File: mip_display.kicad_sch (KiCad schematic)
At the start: 16 parts, among them IC21 LSF0204GU12X, J5 1-2328702-0, J6 2328702-4, Q4 BC847

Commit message: Changed hand soldered footprints to normal footprints
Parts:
- C79, C82, C85, C86: footprint Capacitor_SMD:C_0603_1608Metric_Pad1.08x0.95mm_HandSolder -> Capacitor_SMD:C_0603_1608Metric
- C80, C81, C84: footprint Capacitor_SMD:C_0402_1005Metric_Pad0.74x0.62mm_HandSolder -> Capacitor_SMD:C_0402_1005Metric
- R46: footprint Resistor_SMD:R_0402_1005Metric_Pad0.72x0.64mm_HandSolder -> Resistor_SMD:R_0402_1005Metric
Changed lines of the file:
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@@
 			)
 		)
-		(property "Footprint" "Capacitor_SMD:C_0402_1005Metric_Pad0.74x0.62mm_HandSolder"
+		(property "Footprint" "Capacitor_SMD:C_0402_1005Metric"
 			(at 200.9648 125.73 0)
 			(effects
@@
 			)
 		)
-		(property "Footprint" "Capacitor_SMD:C_0402_1005Metric_Pad0.74x0.62mm_HandSolder"
+		(property "Footprint" "Capacitor_SMD:C_0402_1005Metric"
 			(at 150.1648 115.57 0)
 			(effects
@@
 			)
 		)
-		(property "Footprint" "Capacitor_SMD:C_0603_1608Metric_Pad1.08x0.95mm_HandSolder"
+		(property "Footprint" "Capacitor_SMD:C_0603_1608Metric"
 			(at 137.4648 115.57 0)
 			(effects
@@
 			)
 		)
-		(property "Footprint" "Capacitor_SMD:C_0402_1005Metric_Pad0.74x0.62mm_HandSolder"
+		(property "Footprint" "Capacitor_SMD:C_0402_1005Metric"
 			(at 80.9752 132.08 0)
 			(effects
@@
 			)
 		)
-		(property "Footprint" "Capacitor_SMD:C_0603_1608Metric_Pad1.08x0.95mm_HandSolder"
+		(property "Footprint" "Capacitor_SMD:C_0603_1608Metric"
 			(at 90.4748 124.46 0)
 			(effects
@@
 			)
 		)
-		(property "Footprint" "Capacitor_SMD:C_0603_1608Metric_Pad1.08x0.95mm_HandSolder"
+		(property "Footprint" "Capacitor_SMD:C_0603_1608Metric"
 			(at 101.9048 124.46 0)
 			(effects
@@
 			)
 		)
-		(property "Footprint" "Capacitor_SMD:C_0603_1608Metric_Pad1.08x0.95mm_HandSolder"
+		(property "Footprint" "Capacitor_SMD:C_0603_1608Metric"
 			(at 212.3948 125.73 0)
 			(effects
@@
 			)
 		)
-		(property "Footprint" "Resistor_SMD:R_0402_1005Metric_Pad0.72x0.64mm_HandSolder"
+		(property "Footprint" "Resistor_SMD:R_0402_1005Metric"
 			(at 100.33 71.882 90)
 			(effects

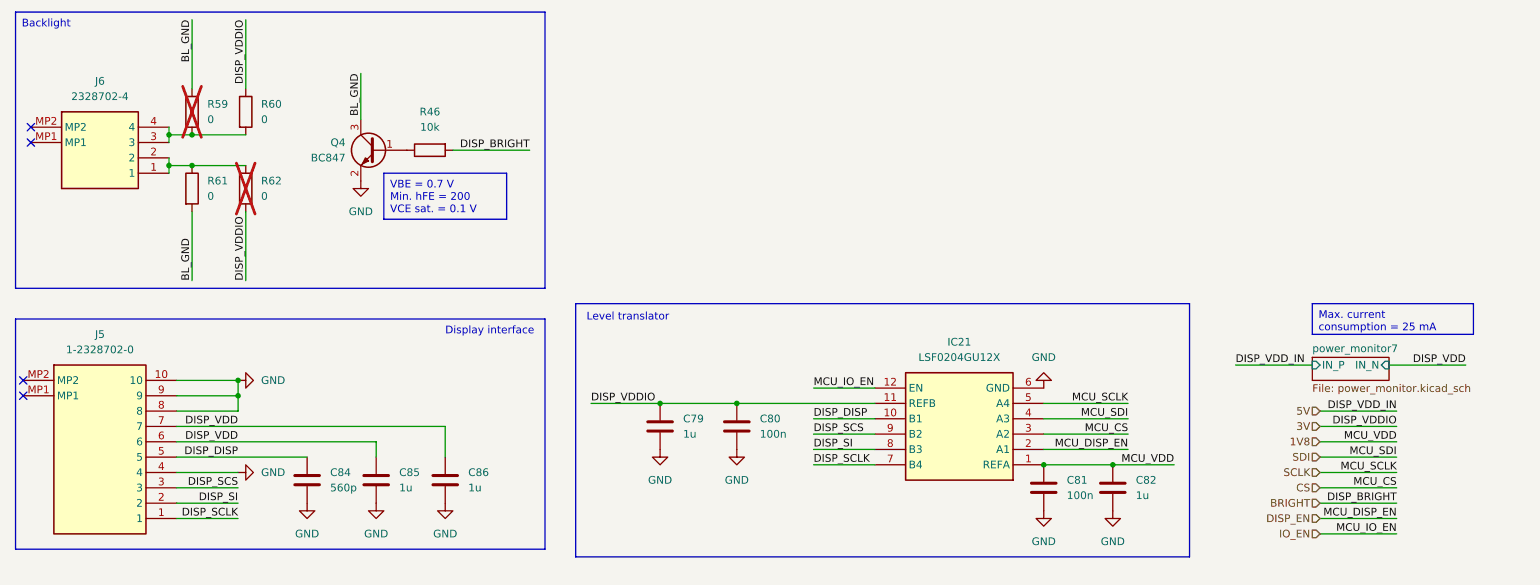
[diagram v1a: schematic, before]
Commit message: Remove RF netclass from a net in gps sheet; Monitor DISP_VDDIO instead of DISP_VDD; Correct constraints
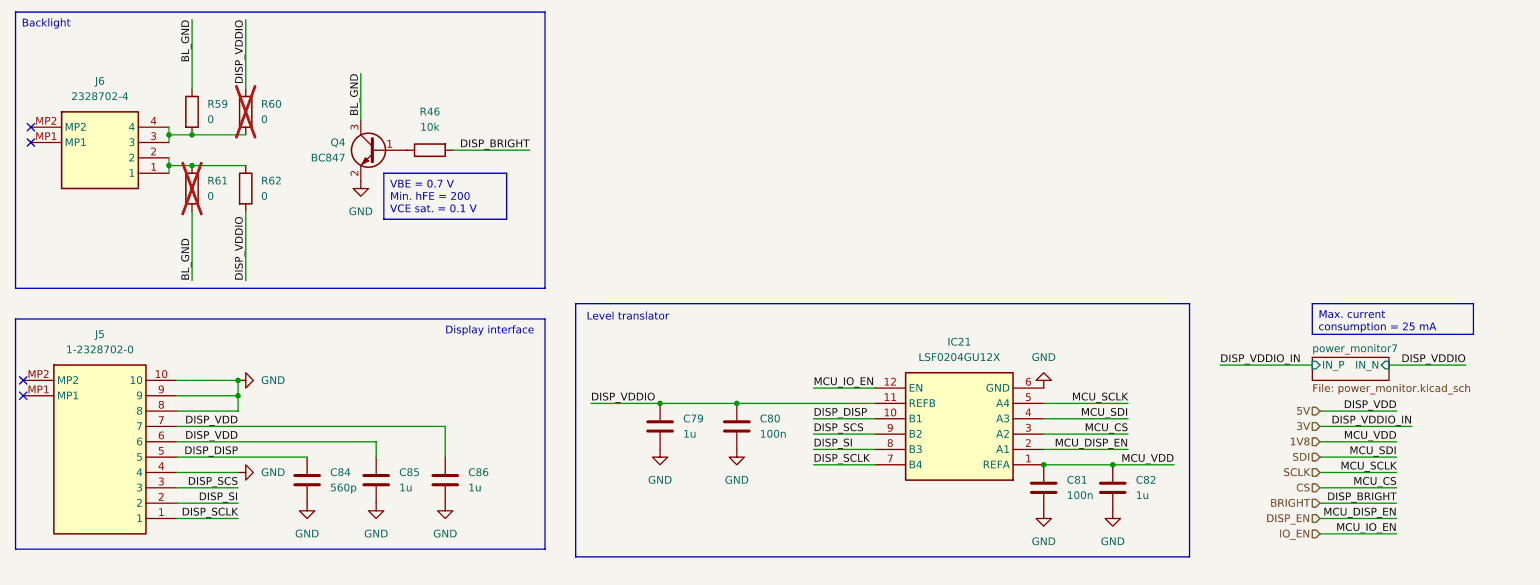
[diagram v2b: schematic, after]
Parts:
- R59, R62: now fitted
- R60, R61: now not fitted
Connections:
- net DISP_VDD is gone; now on net 5V: C85.2, C86.2, J5.6, J5.7
- net 3V: no longer C79.2, C80.2, IC21.11 (REFB), R60.1, R62.2
- new net DISP_VDDIO: C79.2, C80.2, IC21.11 (REFB), R60.1, R62.2
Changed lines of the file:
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@@
 	(wire
 		(pts
-			(xy 233.68 109.22) (xy 246.38 109.22)
+			(xy 231.14 109.22) (xy 246.38 109.22)
 		)
 		(stroke
@@
 	(wire
 		(pts
-			(xy 247.65 119.38) (xy 260.35 119.38)
+			(xy 247.65 119.38) (xy 262.89 119.38)
 		)
 		(stroke
@@
 		)
 	)
-	(label "DISP_VDD"
+	(label "DISP_VDDIO"
 		(at 271.78 109.22 180)
 		(fields_autoplaced yes)
@@
 		)
 	)
-	(label "DISP_VDD_IN"
-		(at 233.68 109.22 0)
+	(label "DISP_VDDIO_IN"
+		(at 231.14 109.22 0)
 		(fields_autoplaced yes)
 		(effects
@@
 		)
 	)
-	(label "DISP_VDD_IN"
+	(label "DISP_VDD"
 		(at 260.35 116.84 180)
 		(fields_autoplaced yes)
@@
 		)
 	)
-	(label "DISP_VDDIO"
-		(at 260.35 119.38 180)
+	(label "DISP_VDDIO_IN"
+		(at 262.89 119.38 180)
 		(fields_autoplaced yes)
 		(effects
@@
 		(in_bom yes)
 		(on_board yes)
-		(dnp no)
+		(dnp yes)
 		(fields_autoplaced yes)
 		(property "Reference" "R61"
@@
 		(in_bom yes)
 		(on_board yes)
-		(dnp yes)
+		(dnp no)
 		(fields_autoplaced yes)
 		(property "Reference" "R62"
@@
 		(in_bom yes)
 		(on_board yes)
-		(dnp no)
+		(dnp yes)
 		(fields_autoplaced yes)
 		(property "Reference" "R60"
@@
 		(in_bom yes)
 		(on_board yes)
-		(dnp yes)
+		(dnp no)
 		(fields_autoplaced yes)
 		(property "Reference" "R59"

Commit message: Finished hardware design
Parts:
- removed J5: 1-2328702-0, 1-2328702-0:123287020, symbol 1-2328702-0:1-2328702-0
- removed J6: 2328702-4, 2328702-4:23287024, symbol 2328702-4:2328702-4
- added J3: 1-2328702-0, 1-2328702-0:123287020, symbol 1-2328702-0:1-2328702-0
- added J4: 2328702-4, 2328702-4:23287024, symbol 2328702-4:2328702-4
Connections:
- net 5V: now also J3.4, J3.5
- net DISP_DISP: now also J3.6
- net DISP_SCLK: now also J3.10
- net DISP_SCS: now also J3.8
- net DISP_SI: now also J3.9
- net GND: now also J3.1, J3.2, J3.3, J3.7
- net at R61.1, R62.1: now also J4.3, J4.4
- net at R59.2, R60.2: now also J4.1, J4.2
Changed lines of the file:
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@@
 	)
 	(no_connect
-		(at 34.29 72.39)
+		(at 34.29 77.47)
 	)
 	(no_connect
-		(at 33.02 114.3)
+		(at 33.02 134.62)
 	)
 	(no_connect
-		(at 33.02 111.76)
+		(at 33.02 132.08)
 	)
 	(no_connect
-		(at 34.29 69.85)
+		(at 34.29 74.93)
 	)
 	(wire
@@
 	)
 	(symbol
-		(lib_id "2328702-4:2328702-4")
-		(at 34.29 69.85 0)
+		(lib_id "1-2328702-0:1-2328702-0")
+		(at 33.02 134.62 0)
+		(mirror x)
 		(unit 1)
 		(exclude_from_sim no)
@@
 		(on_board yes)
 		(dnp no)
-		(fields_autoplaced yes)
-		(property "Reference" "J6"
-			(at 45.72 62.23 0)
+		(property "Reference" "J3"
+			(at 45.72 142.24 0)
 			(effects
 				(font
@@
 			)
 		)
-		(property "Value" "2328702-4"
-			(at 45.72 64.77 0)
+		(property "Value" "1-2328702-0"
+			(at 45.72 139.7 0)
 			(effects
 				(font
@@
 			)
 		)
-		(property "Footprint" "2328702-4:23287024"
-			(at 53.34 164.77 0)
+		(property "Footprint" "1-2328702-0:123287020"
+			(at 54.61 39.7 0)
 			(effects
 				(font
@@
 			)
 		)
-		(property "Datasheet" "https://www.te.com/commerce/DocumentDelivery/DDEController?Action=srchrtrv&DocNm=1-1773959-7-FPC-Connectors-CN&DocType=Data%20Sheet&DocLang=Chinese (Simplified)&PartCntxt=2328702-4&DocFormat=pdf"
-			(at 53.34 264.77 0)
+		(property "Datasheet" "https://datasheet.datasheetarchive.com/originals/distributors/DKDS42/DSANUWW0052081.pdf"
+			(at 54.61 -60.3 0)
 			(effects
 				(font
@@
 			)
 		)
-		(property "Description" "Body Features: Actuator Color Black | Primary Product Color Natural | Configuration Features: PCB Mount Orientation Right Angle | Number of Rows 1 | Compatible With Wire & Cable Type FFC | Number of Positions 4 | Compatible With Wire & Cable Type FPC | Contact Features: Contact Current Rating (Max) .5 AMP | Contact Mating Area Plating Material Gold | Contact Base Material Copper Alloy | Contact Mating Location Dual Side | PCB Contact Termination Area Plating Material Gold | Contact Shape & Form Standard Fla"
-			(at 34.29 69.85 0)
+		(property "Description" "AMP - TE CONNECTIVITY - 1-2328702-0 - CONNECTOR, FPC, R/A, 10POS, 1ROW, 0.5MM"
+			(at 33.02 134.62 0)
 			(effects
 				(font
@@
 		)
 		(property "Height" "1.05"
-			(at 53.34 464.77 0)
+			(at 54.61 -260.3 0)
 			(effects
 				(font
@@
 			)
 		)
-		(property "Mouser Part Number" "571-2328702-4"
-			(at 53.34 564.77 0)
+		(property "Mouser Part Number" "571-1-2328702-0"
+			(at 54.61 -360.3 0)
 			(effects
 				(font
@@
 			)
 		)
-		(property "Mouser Price/Stock" "https://www.mouser.co.uk/ProductDetail/TE-Connectivity/2328702-4?qs=w%2Fv1CP2dgqrq1I7zgm1Wkw%3D%3D"
-			(at 53.34 664.77 0)
+		(property "Mouser Price/Stock" "https://www.mouser.co.uk/ProductDetail/TE-Connectivity/1-2328702-0?qs=w%2Fv1CP2dgqo2Dg4sQQnZ1g%3D%3D"
+			(at 54.61 -460.3 0)
 			(effects
 				(font
@@
 		)
 		(property "Manufacturer_Name" "TE Connectivity"
-			(at 53.34 764.77 0)
+			(at 54.61 -560.3 0)
 			(effects
 				(font
@@
 			)
 		)
-		(property "Manufacturer_Part_Number" "2328702-4"
-			(at 53.34 864.77 0)
+		(property "Manufacturer_Part_Number" "1-2328702-0"
+			(at 54.61 -660.3 0)
 			(effects
 				(font
@@
 		(pin "MP1"
 		)
-		(pin "MP2"
+		(pin "9"
+		)
+		(pin "6"
+		)
+		(pin "5"
 		)
 		(pin "1"
 		)
-		(pin "4"
+		(pin "3"
+		)
+		(pin "MP2"
+		)
+		(pin "7"
 		)
 		(pin "2"
 		)
-		(pin "3"
+		(pin "4"
+		)
+		(pin "8"
+		)
+		(pin "10"
 		)
 		(instances
 			(project "open-running-watch"
 				(path "/3291c566-6d99-47d5-9732-6d96e6cc4ea8/72b765b4-9cf7-4339-9de5-5aa831039a5b"
-					(reference "J6")
+					(reference "J3")
 					(unit 1)
 				)
@@
 	)
 	(symbol
-		(lib_id "1-2328702-0:1-2328702-0")
-		(at 33.02 111.76 0)
-		(unit 1)
-		(exclude_from_sim no)
-		(in_bom yes)
-		(on_board yes)
-		(dnp no)
-		(fields_autoplaced yes)
-		(property "Reference" "J5"
-			(at 45.72 104.14 0)
-			(effects
-				(font
-					(size 1.27 1.27)
-				)
-			)
-		)
-		(property "Value" "1-2328702-0"
-			(at 45.72 106.68 0)
-			(effects
-				(font
-					(size 1.27 1.27)
-				)
-			)
-		)
-		(property "Footprint" "1-2328702-0:123287020"
-			(at 54.61 206.68 0)
-			(effects
-				(font
-					(size 1.27 1.27)
-				)
-				(justify left top)
-				(hide yes)
-			)
-		)
-		(property "Datasheet" "https://datasheet.datasheetarchive.com/originals/distributors/DKDS42/DSANUWW0052081.pdf"
-			(at 54.61 306.68 0)
-			(effects
-				(font
-					(size 1.27 1.27)
-				)
-				(justify left top)
-				(hide yes)
-			)
-		)
-		(property "Description" "AMP - TE CONNECTIVITY - 1-2328702-0 - CONNECTOR, FPC, R/A, 10POS, 1ROW, 0.5MM"
-			(at 33.02 111.76 0)
-			(effects
-				(font
-					(size 1.27 1.27)
-				)
-				(hide yes)
-			)
-		)
-		(property "Height" "1.05"
-			(at 54.61 506.68 0)
-			(effects
-				(font
-					(size 1.27 1.27)
-				)
-				(justify left top)
-				(hide yes)
-			)
-		)
-		(property "Mouser Part Number" "571-1-2328702-0"
-			(at 54.61 606.68 0)
-			(effects
-				(font
-					(size 1.27 1.27)
-				)
-				(justify left top)
-				(hide yes)
-			)
-		)
-		(property "Mouser Price/Stock" "https://www.mouser.co.uk/ProductDetail/TE-Connectivity/1-2328702-0?qs=w%2Fv1CP2dgqo2Dg4sQQnZ1g%3D%3D"
-			(at 54.61 706.68 0)
-			(effects
-				(font
-					(size 1.27 1.27)
-				)
-				(justify left top)
-				(hide yes)
-			)
-		)
-		(property "Manufacturer_Name" "TE Connectivity"
-			(at 54.61 806.68 0)
-			(effects
-				(font
-					(size 1.27 1.27)
-				)
-				(justify left top)
-				(hide yes)
-			)
-		)
-		(property "Manufacturer_Part_Number" "1-2328702-0"
-			(at 54.61 906.68 0)
-			(effects
-				(font
-					(size 1.27 1.27)
-				)
-				(justify left top)
-				(hide yes)
-			)
-		)
-		(pin "MP1"
-		)
-		(pin "9"
-		)
-		(pin "6"
-		)
-		(pin "5"
-		)
-		(pin "1"
-		)
-		(pin "3"
-		)
-		(pin "MP2"
-		)
-		(pin "7"
-		)
-		(pin "2"
-		)
-		(pin "4"
-		)
-		(pin "8"
-		)
-		(pin "10"
-		)
-		(instances
-			(project "open-running-watch"
-				(path "/3291c566-6d99-47d5-9732-6d96e6cc4ea8/72b765b4-9cf7-4339-9de5-5aa831039a5b"
-					(reference "J5")
-					(unit 1)
-				)
-			)
-		)
-	)
-	(symbol
 		(lib_id "power:GND")
 		(at 80.01 132.08 0)
@@
 					(unit 1)
 				)
+			)
+		)
+	)
+	(symbol
+		(lib_id "2328702-4:2328702-4")
+		(at 34.29 77.47 0)
+		(mirror x)
+		(unit 1)
+		(exclude_from_sim no)
+		(in_bom yes)
+		(on_board yes)
+		(dnp no)
+		(property "Reference" "J4"
+			(at 45.72 85.09 0)
+			(effects
+				(font
+					(size 1.27 1.27)
+				)
+			)
+		)
+		(property "Value" "2328702-4"
+			(at 45.72 82.55 0)
+			(effects
+				(font
+					(size 1.27 1.27)
+				)
+			)
+		)
+		(property "Footprint" "2328702-4:23287024"
+			(at 53.34 -17.45 0)
+			(effects
+				(font
+					(size 1.27 1.27)
+				)
+				(justify left top)
+				(hide yes)
+			)
+		)
+		(property "Datasheet" "https://www.te.com/commerce/DocumentDelivery/DDEController?Action=srchrtrv&DocNm=1-1773959-7-FPC-Connectors-CN&DocType=Data%20Sheet&DocLang=Chinese (Simplified)&PartCntxt=2328702-4&DocFormat=pdf"
+			(at 53.34 -117.45 0)
+			(effects
+				(font
+					(size 1.27 1.27)
+				)
+				(justify left top)
+				(hide yes)
+			)
+		)
+		(property "Description" "Body Features: Actuator Color Black | Primary Product Color Natural | Configuration Features: PCB Mount Orientation Right Angle | Number of Rows 1 | Compatible With Wire & Cable Type FFC | Number of Positions 4 | Compatible With Wire & Cable Type FPC | Contact Features: Contact Current Rating (Max) .5 AMP | Contact Mating Area Plating Material Gold | Contact Base Material Copper Alloy | Contact Mating Location Dual Side | PCB Contact Termination Area Plating Material Gold | Contact Shape & Form Standard Fla"
+			(at 34.29 77.47 0)
+			(effects
+				(font
+					(size 1.27 1.27)
+				)
+				(hide yes)
+			)
+		)
+		(property "Height" "1.05"
+			(at 53.34 -317.45 0)
+			(effects
+				(font
+					(size 1.27 1.27)
+				)
+				(justify left top)
+				(hide yes)
+			)
+		)
+		(property "Mouser Part Number" "571-2328702-4"
+			(at 53.34 -417.45 0)
+			(effects
+				(font
+					(size 1.27 1.27)
+				)
+				(justify left top)
+				(hide yes)
+			)
+		)
+		(property "Mouser Price/Stock" "https://www.mouser.co.uk/ProductDetail/TE-Connectivity/2328702-4?qs=w%2Fv1CP2dgqrq1I7zgm1Wkw%3D%3D"
+			(at 53.34 -517.45 0)
+			(effects
+				(font
+					(size 1.27 1.27)
+				)
+				(justify left top)
+				(hide yes)
+			)
+		)
+		(property "Manufacturer_Name" "TE Connectivity"
+			(at 53.34 -617.45 0)
+			(effects
+				(font
+					(size 1.27 1.27)
+				)
+				(justify left top)
+				(hide yes)
+			)
+		)
+		(property "Manufacturer_Part_Number" "2328702-4"
+			(at 53.34 -717.45 0)
+			(effects
+				(font
+					(size 1.27 1.27)
+				)
+				(justify left top)
+				(hide yes)
+			)
+		)
+		(pin "MP1"
+		)
+		(pin "MP2"
+		)
+		(pin "1"
+		)
+		(pin "4"
+		)
+		(pin "2"
+		)
+		(pin "3"
+		)
+		(instances
+			(project "open-running-watch"
+				(path "/3291c566-6d99-47d5-9732-6d96e6cc4ea8/72b765b4-9cf7-4339-9de5-5aa831039a5b"
+					(reference "J4")
+					(unit 1)
+				)

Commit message: Remove additional spaces in Manufacturer_Part_Number field
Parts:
- C80, C81: Manufacturer_Part_Number GRM155R71A104MA01D -> GRM155R71A104MA01D
- R46: Manufacturer_Part_Number RC0402JR-0710KP -> RC0402JR-0710KP
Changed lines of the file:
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@@
 			)
 		)
-		(property "Manufacturer_Part_Number" "GRM155R71A104MA01D "
+		(property "Manufacturer_Part_Number" "GRM155R71A104MA01D"
 			(at 201.93 129.54 0)
 			(effects
@@
 			)
 		)
-		(property "Manufacturer_Part_Number" "GRM155R71A104MA01D "
+		(property "Manufacturer_Part_Number" "GRM155R71A104MA01D"
 			(at 151.13 119.38 0)
 			(effects
@@
 			)
 		)
-		(property "Manufacturer_Part_Number" " RC0402JR-0710KP"
+		(property "Manufacturer_Part_Number" "RC0402JR-0710KP"
 			(at 100.33 73.66 0)
 			(effects

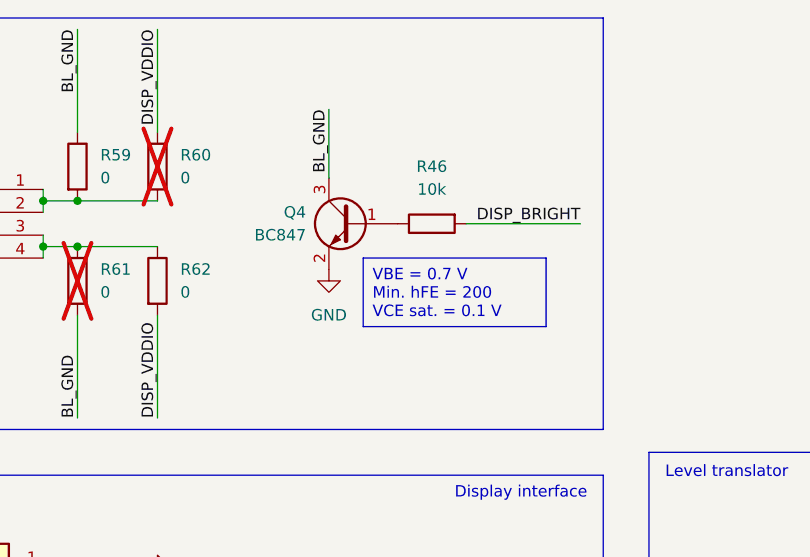
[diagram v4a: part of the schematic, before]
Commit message: Changed transistor used in display backlight switch
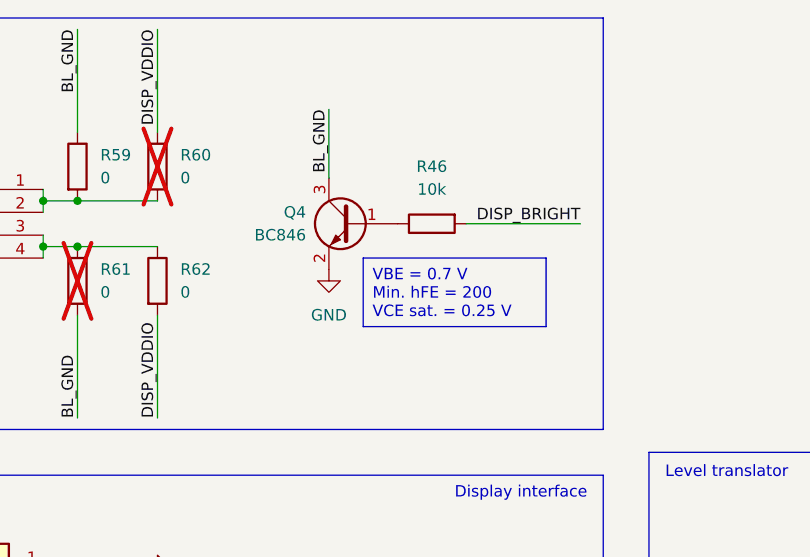
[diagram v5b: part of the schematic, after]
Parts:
- removed Q4: BC847, Package_TO_SOT_SMD:SOT-23, symbol Transistor_BJT:BC847
- added Q4: BC846, Package_TO_SOT_SMD:SOT-23, symbol Transistor_BJT:BC846
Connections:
- net BL_GND: now also Q4.3 (C)
- net GND: now also Q4.2 (E)
- net at R46.1: now also Q4.1 (B)
